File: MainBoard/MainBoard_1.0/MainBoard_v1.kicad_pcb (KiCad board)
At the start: 2 copper layers, 120 x 80 mm, 166 parts, among them J1 ILG, J10 SH, J11 SH, J12 SH, J13 FFC, J14 SH, J2 SH, J3 STDC14, J4 PA, J5 Micro_SD_Card_Det_Hirose_DM3AT, J6 SH, J7 ENC, J8 ENC, J9 PA, Q1 AON7400B, Q10 IRLML6344, Q2 AON7400B, Q3 AON7400B, Q4 AON7400B, Q5 AON7400B, Q6 AON7400B, Q7 2N7002K, Q8 AON7400B, Q9 AON7400B, SW1 SKRPACE010, SW2 SSSS213202, SW3 FR01SC16P-S, SW4 SKRHAAE010, U1 SI7469DP-T1-GE3, U10 DRV8701E, U11 MMC5983MA, U2 LT1963A-TSSOP, U3 TPS62143, U4 ECS-2520S33, U5 INA260, U6 DRV8701E, U7 ICM20648, U8 STM32F469VG, U9 INA260

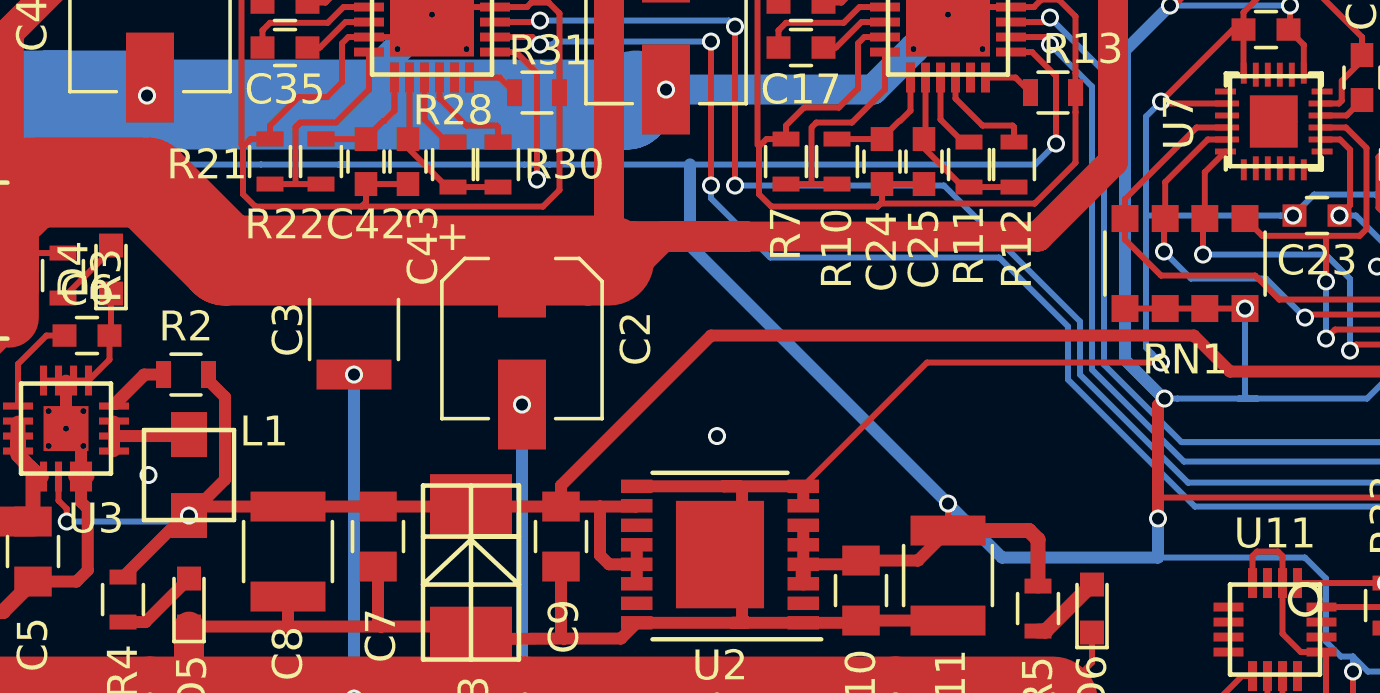
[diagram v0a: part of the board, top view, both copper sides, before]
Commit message: change capaciter size
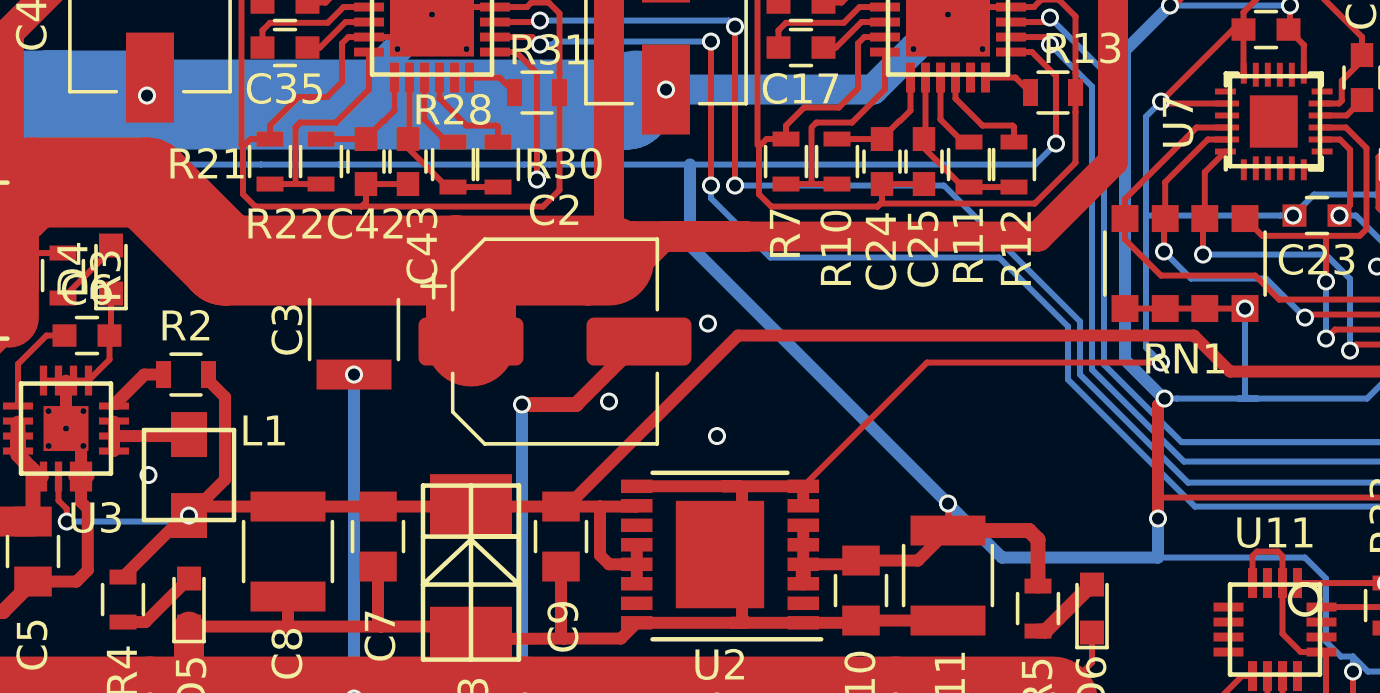
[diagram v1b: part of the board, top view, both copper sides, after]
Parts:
- C2: footprint Capacitors_SMD:CP_Elec_5x5.8 -> Capacitor_SMD:CP_Elec_6.3x5.9
- moved C2 1.10 mm to (120.5, 123.8), turned to 0 degrees
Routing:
- net GND: track 931.1 -> 935.8 mm, vias 122 -> 124
- net +BATT: track 153.7 -> 156.6 mm

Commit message: fixed
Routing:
- net GND: track 935.8 -> 938.0 mm, vias 124 -> 130

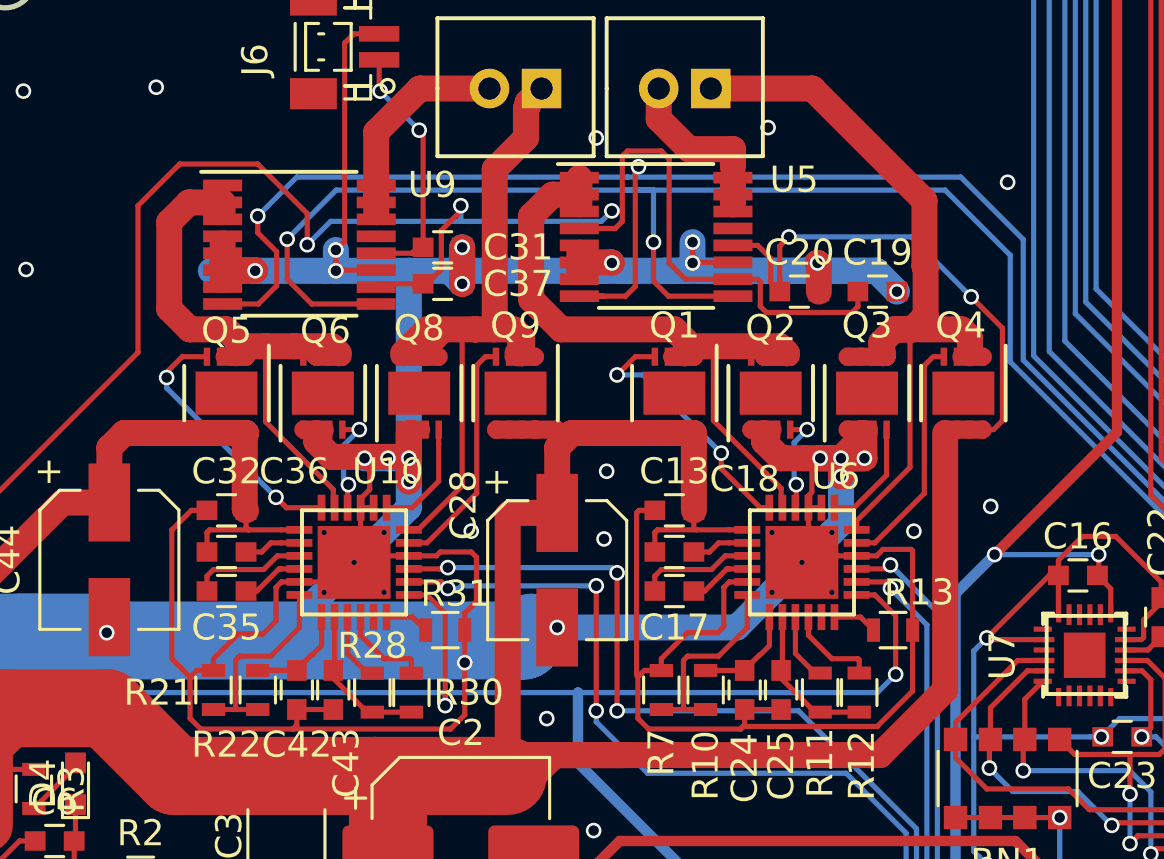
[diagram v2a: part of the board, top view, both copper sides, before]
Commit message: change FET footprint
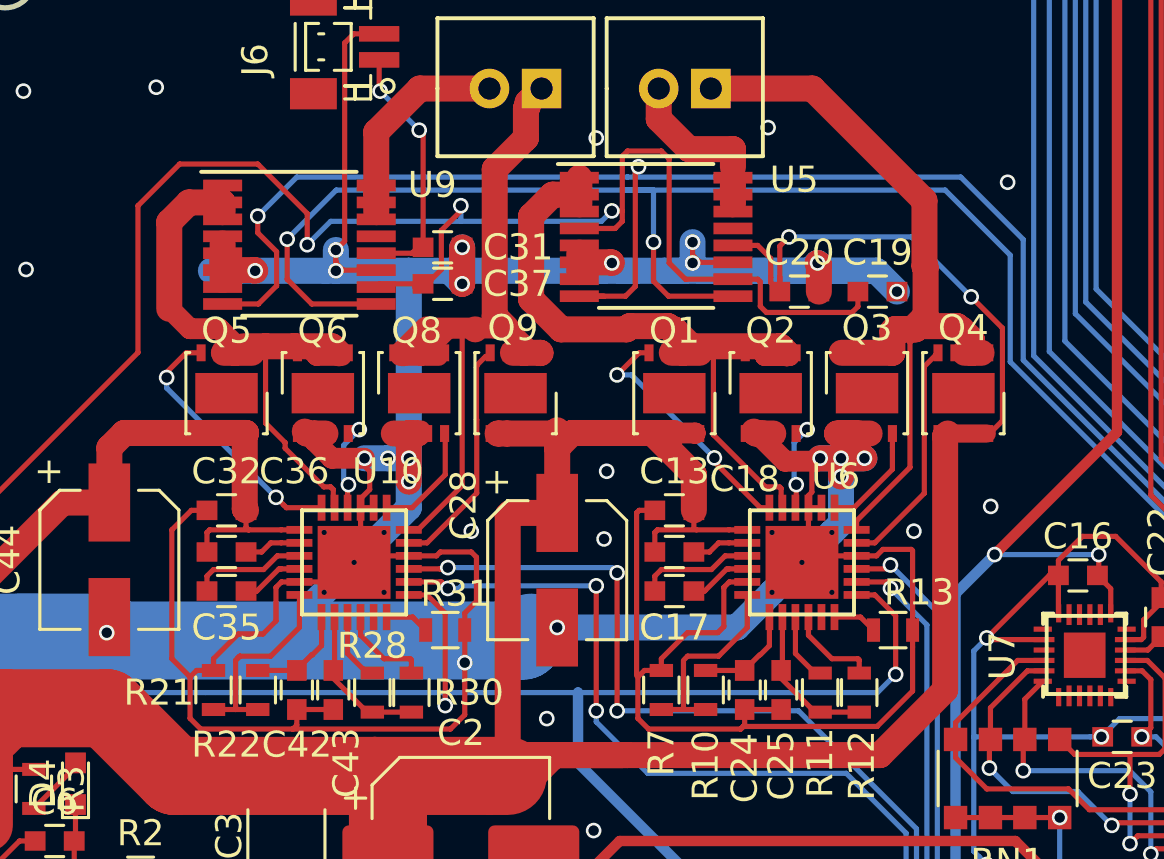
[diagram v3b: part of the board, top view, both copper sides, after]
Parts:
- Q1, Q2, Q3, Q4, Q5, Q6, Q8, Q9: footprint Housings_DFN_QFN:DFN-8-1EP_3x3mm_Pitch0.5mm -> Package_DFN_QFN:DFN-8-1EP_3x3mm_P0.65mm_EP1.55x2.4mm
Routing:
- net GND: track 938.0 -> 933.7 mm
- net Net-(Q1-Pad1): track 30.7 -> 28.2 mm
- net Net-(J9-Pad1): track 30.3 -> 28.9 mm

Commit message: fixed
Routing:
- net GND: track 933.7 -> 936.5 mm, vias 130 -> 132

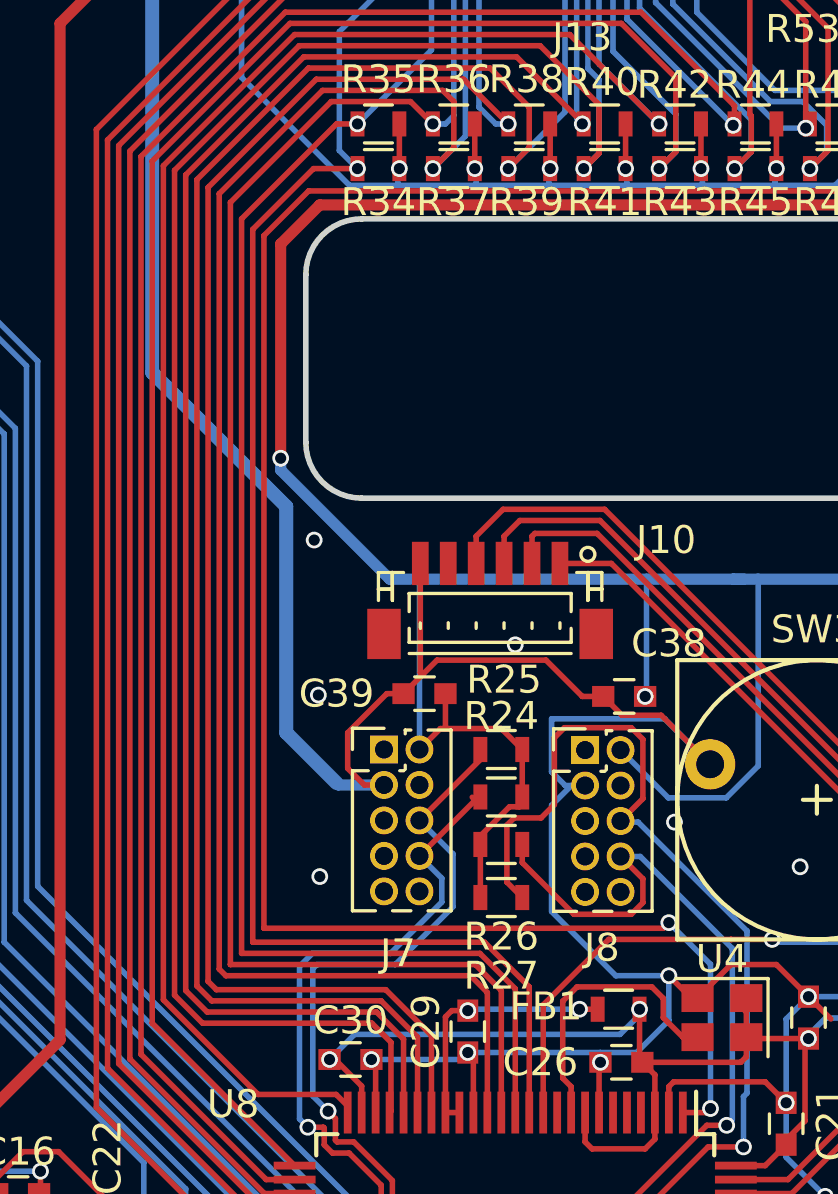
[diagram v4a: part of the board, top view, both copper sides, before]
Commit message: センサの抵抗値などを変更
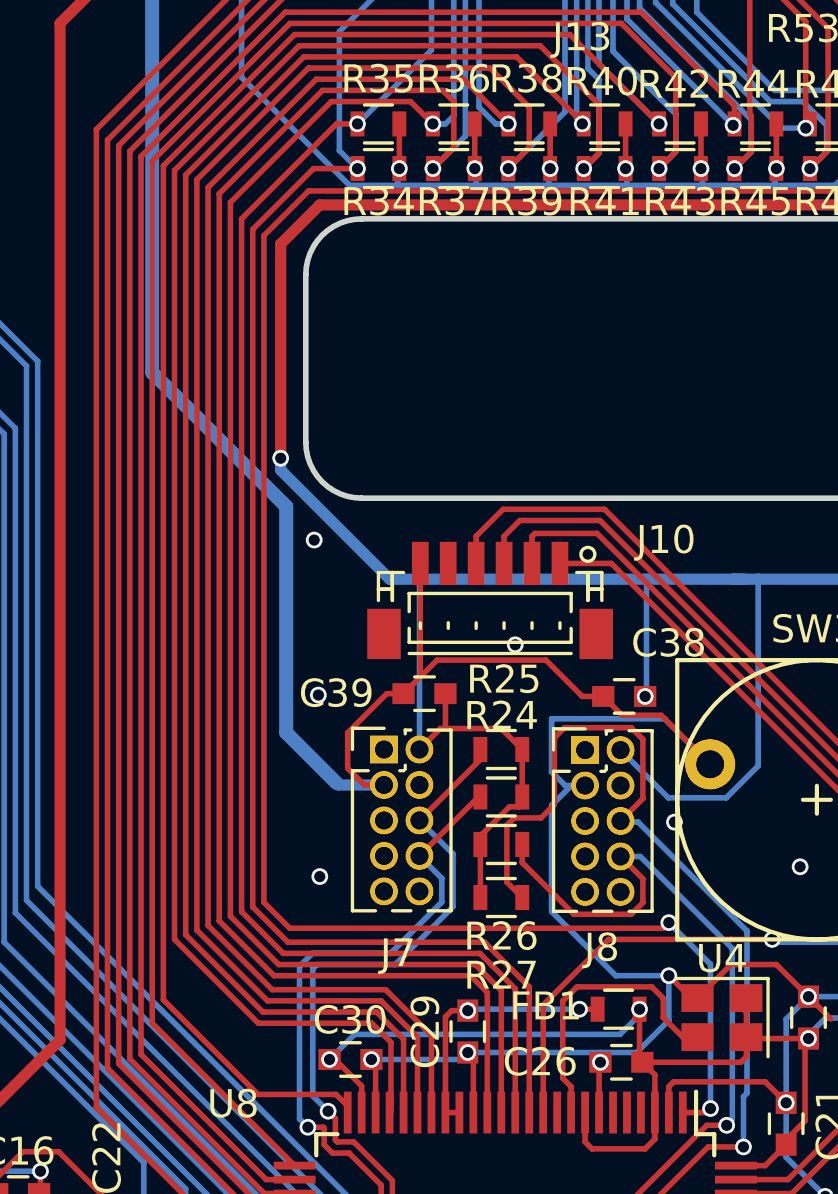
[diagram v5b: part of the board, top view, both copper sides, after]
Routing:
- net AD8: track 75.1 -> 73.9 mm
- net AD6: track 72.0 -> 70.8 mm
- net AD5: track 65.7 -> 64.5 mm
- net AD7: track 69.8 -> 68.7 mm
- net AD4: track 69.2 -> 68.2 mm
- net AD3: track 62.5 -> 61.5 mm
- net AD2: track 57.5 -> 56.7 mm
- net AD1: track 57.3 -> 56.5 mm
- net MAKER1: track 80.0 -> 79.5 mm
